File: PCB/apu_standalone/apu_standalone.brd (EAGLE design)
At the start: 110.5 x 54.4 mm, 95 parts, among them IC1 74AHC573, IC10 DAC, IC11 IS62C1024AL, IC12 ATMEGA2560, IC15 FT232RL, IC2 4050D, IC3 DS1307, IC4 LP298XS, IC5 S-SMP, IC6 S-DSP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

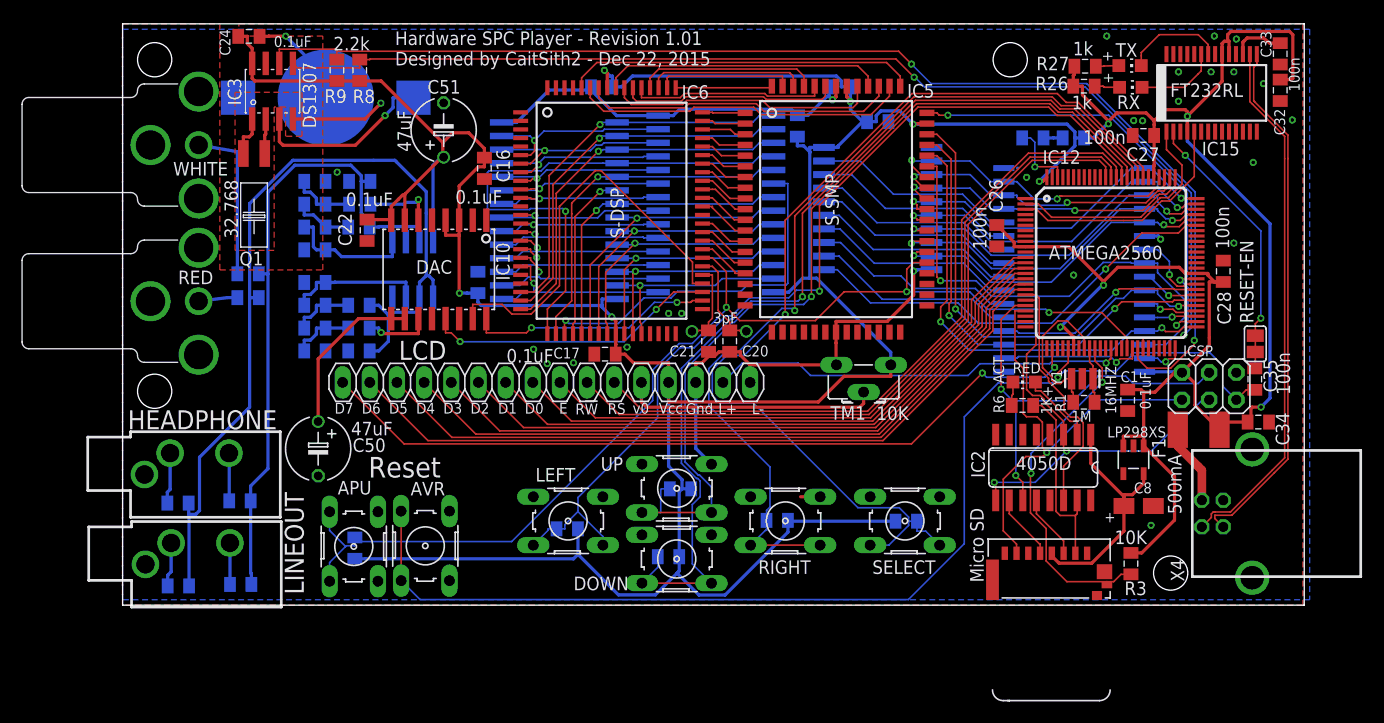
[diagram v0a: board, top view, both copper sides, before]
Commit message: reorganize directory structure
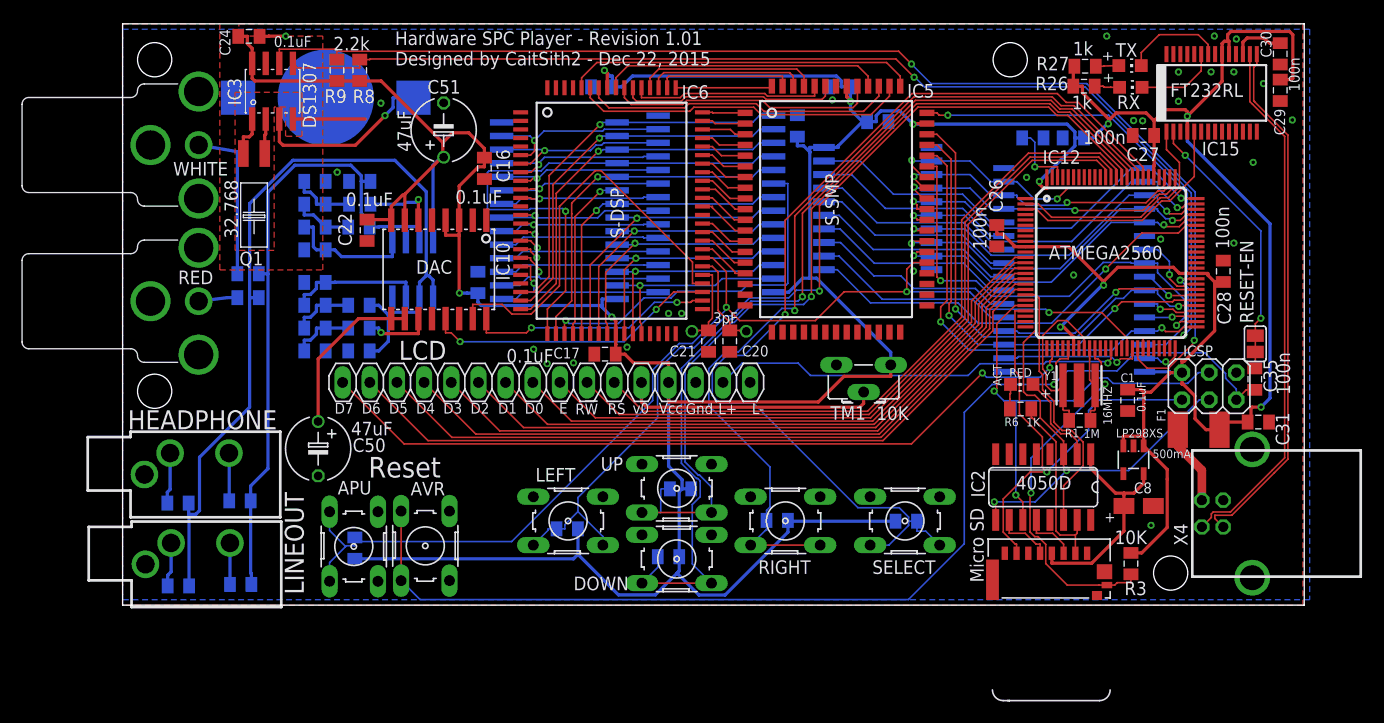
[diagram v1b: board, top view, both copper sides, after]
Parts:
- moved IC2 1.83 mm to (86.1, 11.0)
- moved R1 1.73 mm to (89.5, 17.3)
- moved Y1 0.68 mm to (89.4, 20.6)
- moved R6 0.38 mm to (84.0, 18.3)
- moved ACT 0.32 mm to (84.1, 20.6)
- renumbered C32 to C29, C33 to C30, C34 to C31
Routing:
- net GND: track 104.9 -> 9.20 mm
- net CLK: track 42.4 -> 45.3 mm
- net DI: track 40.5 -> 43.2 mm
- net XTAL3: track 5.30 -> 7.33 mm
- net CS: track 23.2 -> 25.1 mm
- net XTAL4: track 15.1 -> 16.7 mm
- net BUF_LED: track 7.22 -> 8.73 mm
- net VCC: track 467.3 -> 468.6 mm
- net DO: track 43.7 -> 45.0 mm
- net RESET: track 110.1 -> 111.4 mm
- net +3V3: track 22.2 -> 21.0 mm
- net CD: track 32.9 -> 34.0 mm
- net BUF_DI: track 6.00 -> 5.06 mm
- net BUF_CLK: track 6.16 -> 5.40 mm
- net BUF_CS: track 18.2 -> 17.6 mm

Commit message: Change out PTC fuse for better clearance.
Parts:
- F1: device rcl:L1812 -> inductor-neosid:SM-1206
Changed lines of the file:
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@@
 <setting verticaltext="up"/>
 </settings>
-<grid distance="12" unitdist="mil" unit="mm" style="lines" multiple="1" display="yes" altdistance="1" altunitdist="mil" altunit="mil"/>
+<grid distance="12" unitdist="mil" unit="mil" style="lines" multiple="1" display="yes" altdistance="1" altunitdist="mil" altunit="mil"/>
 <layers>
 <layer number="1" name="Top" color="4" fill="1" visible="yes" active="yes"/>
@@
 <attribute name="VALUE" x="114.5168" y="16.185" size="1.27" layer="27" rot="R180"/>
 </element>
-<element name="F1" library="rcl" package="L1812" value="500mA" x="100.6154" y="16.4041" smashed="yes" rot="R180">
-<attribute name="NAME" x="96.7066" y="18.3907" size="0.8128" layer="25" font="vector" ratio="16" rot="R270"/>
-<attribute name="VALUE" x="96.3108" y="13.7457" size="0.8128" layer="25" font="vector" ratio="16"/>
+<element name="F1" library="inductor-neosid" package="SM-1206" value="500mA" x="100.6154" y="16.4041" smashed="yes" rot="R180">
+<attribute name="NAME" x="97.4686" y="17.2731" size="0.8128" layer="25" font="vector" ratio="16" rot="R270"/>
+<attribute name="VALUE" x="98.7492" y="14.6601" size="0.8128" layer="25" font="vector" ratio="16"/>
+<attribute name="OC_NEWARK" value="unknown" x="100.6154" y="16.4041" size="1.778" layer="27" rot="R180" display="off"/>
+<attribute name="MPN" value="" x="100.6154" y="16.4041" size="1.778" layer="27" rot="R180" display="off"/>
+<attribute name="MF" value="" x="100.6154" y="16.4041" size="1.778" layer="27" rot="R180" display="off"/>
+<attribute name="OC_FARNELL" value="unknown" x="100.6154" y="16.4041" size="1.778" layer="27" rot="R180" display="off"/>
 </element>
 <element name="C31" library="apu_pcb" package="C0805" value="100n" x="106.1974" y="17.1196" smashed="yes">
@@
 <wire x1="99.06" y1="21.7424" x2="99.06" y2="20.6625" width="0.3048" layer="1"/>
 <wire x1="99.06" y1="21.7424" x2="99.06" y2="22.8223" width="0.3048" layer="1"/>
-<wire x1="102.5654" y1="16.4041" x2="101.3105" y2="16.4041" width="0.3048" layer="1"/>
+<wire x1="102.2654" y1="16.4041" x2="101.3105" y2="16.4041" width="0.3048" layer="1"/>
 <wire x1="99.06" y1="21.7424" x2="97.9801" y2="21.7424" width="0.3048" layer="1"/>
 <wire x1="99.06" y1="21.7424" x2="97.9801" y2="21.7424" width="0.3048" layer="16"/>
@@
 <wire x1="105.5116" y1="17.4338" x2="105.1974" y2="17.1196" width="0.3048" layer="1"/>
 <wire x1="105.1974" y1="17.1196" x2="103.2809" y2="17.1196" width="0.3048" layer="1"/>
-<wire x1="103.2809" y1="17.1196" x2="102.5654" y2="16.4041" width="0.3048" layer="1"/>
+<wire x1="103.2809" y1="17.1196" x2="102.2654" y2="16.4041" width="0.3048" layer="1"/>
 <wire x1="101.3105" y1="16.4041" x2="100.2792" y2="17.4354" width="0.3048" layer="1"/>
 <wire x1="100.2792" y1="17.4354" x2="100.2792" y2="19.5552" width="0.3048" layer="1"/>
@@
 <contactref element="F1" pad="2"/>
 <contactref element="X4" pad="1"/>
-<wire x1="98.6654" y1="16.4041" x2="98.6654" y2="14.8726" width="0.8128" layer="1"/>
-<wire x1="98.6654" y1="14.8726" x2="100.9168" y2="12.6212" width="0.8128" layer="1"/>
-<wire x1="100.9168" y1="12.6212" x2="100.9168" y2="9.815" width="0.8128" layer="1"/>
+<wire x1="98.9654" y1="16.4041" x2="98.9654" y2="14.1154" width="1.27" layer="1"/>
+<wire x1="98.9654" y1="14.1154" x2="99.9744" y2="13.1064" width="1.27" layer="1"/>
+<wire x1="99.9744" y1="13.1064" x2="100.9168" y2="12.164" width="1.27" layer="1"/>
+<wire x1="100.9168" y1="12.164" x2="100.9168" y2="9.815" width="1.27" layer="1"/>
 </signal>
 <signal name="DTR">
